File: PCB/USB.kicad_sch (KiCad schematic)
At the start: 13 parts, among them U8 LT1963AEST-3.3#TRPBF

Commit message: switching to hall effect for now
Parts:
- removed U8: LT1963AEST-3.3#TRPBF, Package_TO_SOT_SMD:SOT-223-3_TabPin2, symbol Regulator_Linear:LT1963AxST-3.3
- added U?: TLV1117-33, symbol Regulator_Linear:TLV1117-33
- C10, C7: value 10u -> 1u
- R1, R?: value R_US -> 5.1k
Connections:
- net +3.3V: now also U?.2 (VO)
- net +5V: now also U?.3 (VI)
- net GND: now also U?.1 (GND)
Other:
- note added: "5V to 3.3V LDO 1A max, bypass caps from data sheet"
- note removed: "5V to 3.3V LDO for ESP power from USB 1A max, bypass cap values via data sheet"
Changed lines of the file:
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@@
 		)
 	)
-	(text "5V to 3.3V LDO for ESP power from USB\n1A max, bypass cap values via data sheet "
+	(text "5V to 3.3V LDO\n1A max, bypass caps from data sheet"
 		(exclude_from_sim no)
 		(at 189.738 51.181 0)
@@
 	(wire
 		(pts
-			(xy 189.23 40.005) (xy 189.23 41.275)
+			(xy 189.23 37.465) (xy 189.23 41.275)
 		)
 		(stroke
@@
 	(wire
 		(pts
-			(xy 199.39 29.845) (xy 203.2 29.845)
-		)
-		(stroke
-			(width 0)
-			(type default)
-		)
-	)
-	(wire
-		(pts
 			(xy 50.8 33.02) (xy 57.15 33.02)
 		)
@@
 	(wire
 		(pts
+			(xy 196.85 29.845) (xy 203.2 29.845)
+		)
+		(stroke
+			(width 0)
+			(type default)
+		)
+	)
+	(wire
+		(pts
 			(xy 79.375 36.83) (xy 79.375 45.72)
 		)
@@
 	(wire
 		(pts
-			(xy 173.99 29.845) (xy 179.07 29.845)
+			(xy 173.99 29.845) (xy 181.61 29.845)
 		)
 		(stroke
@@
 			)
 		)
-		(property "Value" "R_US"
+		(property "Value" "5.1k"
 			(at 101.6 50.7999 0)
 			(effects
@@
 	)
 	(symbol
-		(lib_id "Regulator_Linear:LT1963AxST-3.3")
-		(at 189.23 32.385 0)
-		(unit 1)
-		(exclude_from_sim no)
-		(in_bom yes)
-		(on_board yes)
-		(dnp no)
-		(fields_autoplaced yes)
-		(property "Reference" "U8"
-			(at 189.23 22.225 0)
-			(effects
-				(font
-					(size 1.27 1.27)
-				)
-			)
-		)
-		(property "Value" "LT1963AEST-3.3#TRPBF"
-			(at 189.23 24.765 0)
-			(effects
-				(font
-					(size 1.27 1.27)
-				)
-			)
-		)
-		(property "Footprint" "Package_TO_SOT_SMD:SOT-223-3_TabPin2"
-			(at 189.23 43.815 0)
-			(effects
-				(font
-					(size 1.27 1.27)
-				)
-				(hide yes)
-			)
-		)
-		(property "Datasheet" "https://www.analog.com/media/en/technical-documentation/data-sheets/1963aff.pdf"
-			(at 189.23 46.355 0)
-			(effects
-				(font
-					(size 1.27 1.27)
-				)
-				(hide yes)
-			)
-		)
-		(property "Description" "3.3V, 1.5A, Low Noise, Fast Transient Response LDO Regulator, SOT-223"
-			(at 189.23 32.385 0)
-			(effects
-				(font
-					(size 1.27 1.27)
-				)
-				(hide yes)
-			)
-		)
-		(property "P/N" "LT1963AEST-3.3#TRPBF"
-			(at 189.23 32.385 0)
-			(effects
-				(font
-					(size 1.27 1.27)
-				)
-				(hide yes)
-			)
-		)
-		(property "Mouser Part Number" "584-1963AEST-3.3TPF"
-			(at 189.23 32.385 0)
-			(effects
-				(font
-					(size 1.27 1.27)
-				)
-				(hide yes)
-			)
-		)
-		(pin "2"
-		)
-		(pin "3"
-		)
-		(pin "1"
-		)
-		(instances
-			(project "OTCboard"
-				(path "/f410b0a0-725c-464e-80be-c0074224226d/df99ead2-0367-4be2-bcea-c49e7e835d17"
-					(reference "U8")
-					(unit 1)
-				)
-			)
-		)
-	)
-	(symbol
 		(lib_id "power:GND")
 		(at 99.695 54.61 0)
@@
 	)
 	(symbol
+		(lib_id "Regulator_Linear:TLV1117-33")
+		(at 189.23 29.845 0)
+		(unit 1)
+		(exclude_from_sim no)
+		(in_bom yes)
+		(on_board yes)
+		(dnp no)
+		(fields_autoplaced yes)
+		(property "Reference" "U?"
+			(at 189.23 22.86 0)
+			(effects
+				(font
+					(size 1.27 1.27)
+				)
+			)
+		)
+		(property "Value" "TLV1117-33"
+			(at 189.23 25.4 0)
+			(effects
+				(font
+					(size 1.27 1.27)
+				)
+			)
+		)
+		(property "Footprint" ""
+			(at 189.23 29.845 0)
+			(effects
+				(font
+					(size 1.27 1.27)
+				)
+				(hide yes)
+			)
+		)
+		(property "Datasheet" "http://www.ti.com/lit/ds/symlink/tlv1117.pdf"
+			(at 189.23 29.845 0)
+			(effects
+				(font
+					(size 1.27 1.27)
+				)
+				(hide yes)
+			)
+		)
+		(property "Description" "800mA Low-Dropout Linear Regulator, 3.3V fixed output, TO-220/TO-252/TO-263/SOT-223"
+			(at 189.23 29.845 0)
+			(effects
+				(font
+					(size 1.27 1.27)
+				)
+				(hide yes)
+			)
+		)
+		(pin "3"
+		)
+		(pin "1"
+		)
+		(pin "2"
+		)
+		(instances
+			(project ""
+				(path "/f410b0a0-725c-464e-80be-c0074224226d/df99ead2-0367-4be2-bcea-c49e7e835d17"
+					(reference "U?")
+					(unit 1)
+				)
+			)
+		)
+	)
+	(symbol
 		(lib_id "Device:LED")
 		(at 267.335 43.815 90)
@@
 			)
 		)
-		(property "Value" "R_US"
+		(property "Value" "5.1k"
 			(at 110.49 50.7999 0)
 			(effects
@@
 			)
 		)
-		(property "Value" "10u"
+		(property "Value" "1u"
 			(at 206.375 36.195 0)
 			(effects
@@
 			)
 		)
-		(property "Value" "10u"
+		(property "Value" "1u"
 			(at 177.165 36.1949 0)
 			(effects

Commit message: cramming for portfolio
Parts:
- J1: renamed from J?; footprint (none) -> Connector_USB:USB_C_Receptacle_GCT_USB4105-xx-A_16P_TopMnt_Horizontal
- R2: renamed from R?; footprint (none) -> Resistor_SMD:R_0603_1608Metric_Pad0.98x0.95mm_HandSolder
- R3: renamed from R1; footprint (none) -> Resistor_SMD:R_0603_1608Metric_Pad0.98x0.95mm_HandSolder
- U2: renamed from U?; footprint (none) -> Package_TO_SOT_SMD:SOT-223
- renumbered C13 to C4, C7 to C5, C10 to C6, D4 to D1, D1 to D2, D2 to D3, D3 to D4, R6 to R4, R7 to R5
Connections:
- net 5V_USB is gone; now on net +5V: C4.1

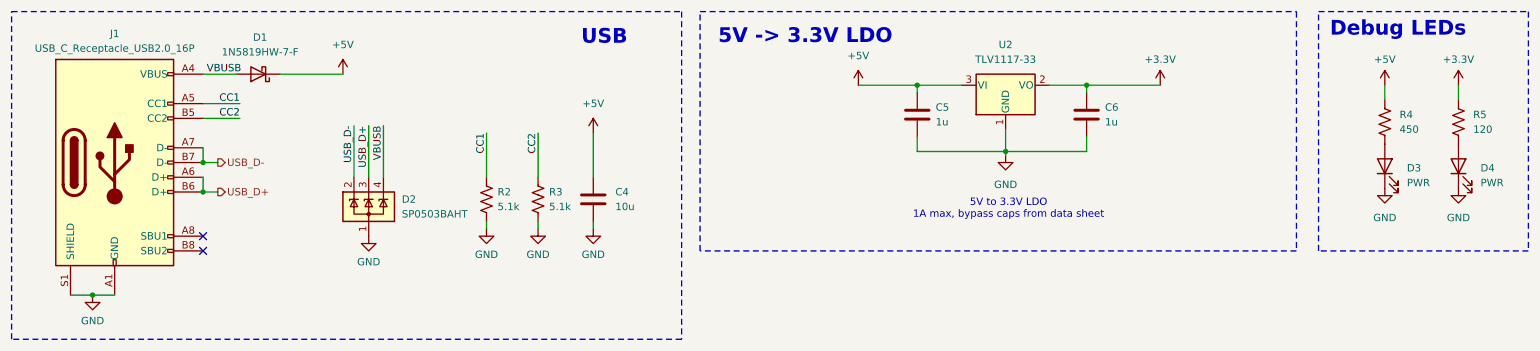
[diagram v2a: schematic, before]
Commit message: only need to find boot and reset footprints
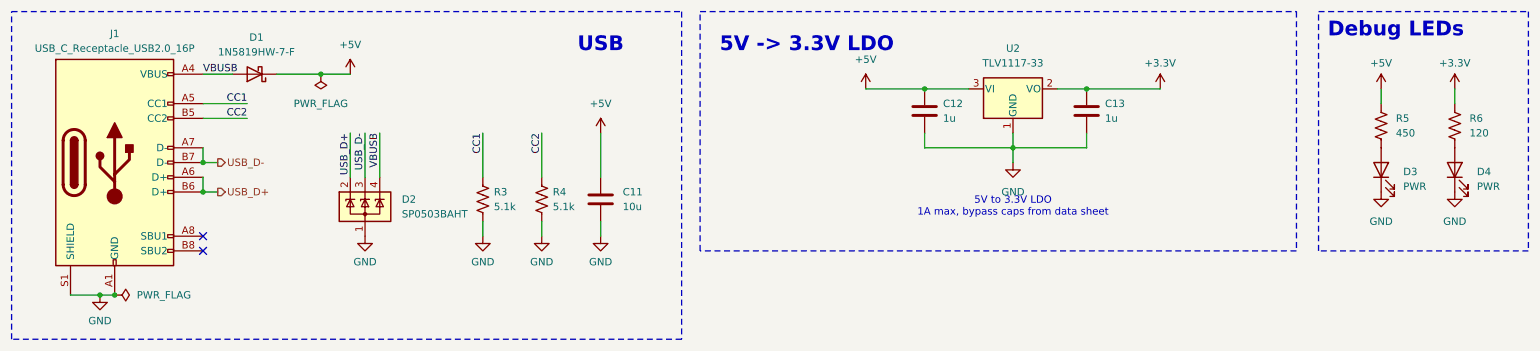
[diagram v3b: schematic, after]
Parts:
- removed D2: SP0503BAHT, Package_TO_SOT_SMD:SOT-143, symbol UTSVT_ICs:SP0503BAH
- added D2: SP0503BAHT, Package_TO_SOT_SMD:SOT-143, symbol Power_Protection:SP0503BAHT
- C12: renamed from C5; footprint Capacitor_SMD:C_0805_2012Metric_Pad1.18x1.45mm_HandSolder -> Capacitor_SMD:C_0603_1608Metric_Pad1.08x0.95mm_HandSolder
- C13: renamed from C6; footprint Capacitor_SMD:C_0805_2012Metric_Pad1.18x1.45mm_HandSolder -> Capacitor_SMD:C_0603_1608Metric_Pad1.08x0.95mm_HandSolder
- renumbered C4 to C11, R2 to R3, R3 to R4, R4 to R5, R5 to R6
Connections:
- net GND: now also D2.1 (A)
- net USB_D+: now also D2.2 (K)
- net USB_D-: now also D2.3 (K)
- net VBUSB: now also D2.4 (K)
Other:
- moved on the sheet: C11, C12, C13, D1, D3, D4, R3, R4, R5, R6, U2

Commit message: changing to wasd
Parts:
- removed U2: TLV1117-33, Package_TO_SOT_SMD:SOT-223, symbol Regulator_Linear:TLV1117-33
- added U2: MCP1826S, Package_TO_SOT_SMD:SOT-223-3_TabPin2, symbol Regulator_Linear:MCP1826S
- C11: renamed from C12; value 1u -> 10u
- C12: renamed from C13; value 1u -> 10u
- R5: value 450 -> 1k
- R6: value 120 -> 1k
- renumbered C11 to C10
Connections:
- net +3.3V: now also U2.3 (VO)
- net +5V: now also U2.1 (VI)
- net GND: now also U2.2 (GND)
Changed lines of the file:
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@@
-	(wire
-		(pts
-			(xy 190.5 43.18) (xy 190.5 40.64)
-		)
-		(stroke
-			(width 0)
-			(type default)
-		)
-	)
 	(wire
 		(pts
@@
 			)
 		)
-		(property "Value" "450"
+		(property "Value" "1k"
 			(at 256.54 38.0999 0)
 			(effects
@@
 			)
 		)
-		(property "Value" "120"
+		(property "Value" "1k"
 			(at 269.24 38.0999 0)
 			(effects
@@
 	)
 	(symbol
-		(lib_id "Regulator_Linear:TLV1117-33")
-		(at 190.5 30.48 0)
-		(unit 1)
-		(exclude_from_sim no)
-		(in_bom yes)
-		(on_board yes)
-		(dnp no)
-		(fields_autoplaced yes)
-		(property "Reference" "U2"
-			(at 190.5 23.495 0)
-			(effects
-				(font
-					(size 1.27 1.27)
-				)
-			)
-		)
-		(property "Value" "TLV1117-33"
-			(at 190.5 26.035 0)
-			(effects
-				(font
-					(size 1.27 1.27)
-				)
-			)
-		)
-		(property "Footprint" "Package_TO_SOT_SMD:SOT-223"
-			(at 190.5 30.48 0)
-			(effects
-				(font
-					(size 1.27 1.27)
-				)
-				(hide yes)
-			)
-		)
-		(property "Datasheet" "http://www.ti.com/lit/ds/symlink/tlv1117.pdf"
-			(at 190.5 30.48 0)
-			(effects
-				(font
-					(size 1.27 1.27)
-				)
-				(hide yes)
-			)
-		)
-		(property "Description" "800mA Low-Dropout Linear Regulator, 3.3V fixed output, TO-220/TO-252/TO-263/SOT-223"
-			(at 190.5 30.48 0)
-			(effects
-				(font
-					(size 1.27 1.27)
-				)
-				(hide yes)
-			)
-		)
-		(pin "3"
-		)
-		(pin "1"
-		)
-		(pin "2"
-		)
-		(instances
-			(project ""
-				(path "/f410b0a0-725c-464e-80be-c0074224226d/df99ead2-0367-4be2-bcea-c49e7e835d17"
-					(reference "U2")
-					(unit 1)
-				)
-			)
-		)
-	)
-	(symbol
 		(lib_id "Device:LED")
 		(at 266.7 44.45 90)
@@
 	)
 	(symbol
+		(lib_id "Regulator_Linear:MCP1826S")
+		(at 190.5 30.48 0)
+		(unit 1)
+		(exclude_from_sim no)
+		(in_bom yes)
+		(on_board yes)
+		(dnp no)
+		(fields_autoplaced yes)
+		(property "Reference" "U2"
+			(at 190.5 24.13 0)
+			(effects
+				(font
+					(size 1.27 1.27)
+				)
+			)
+		)
+		(property "Value" "MCP1826S"
+			(at 190.5 26.67 0)
+			(effects
+				(font
+					(size 1.27 1.27)
+				)
+			)
+		)
+		(property "Footprint" "Package_TO_SOT_SMD:SOT-223-3_TabPin2"
+			(at 187.96 26.67 0)
+			(effects
+				(font
+					(size 1.27 1.27)
+				)
+				(hide yes)
+			)
+		)
+		(property "Datasheet" "http://ww1.microchip.com/downloads/en/DeviceDoc/22057B.pdf"
+			(at 190.5 24.13 0)
+			(effects
+				(font
+					(size 1.27 1.27)
+				)
+				(hide yes)
+			)
+		)
+		(property "Description" "1000mA, Low-Voltage, Low Quiescent Current LDO Regulator, SOT-223, TO-220, TO-263"
+			(at 190.5 30.48 0)
+			(effects
+				(font
+					(size 1.27 1.27)
+				)
+				(hide yes)
+			)
+		)
+		(pin "2"
+		)
+		(pin "1"
+		)
+		(pin "3"
+		)
+		(instances
+			(project ""
+				(path "/f410b0a0-725c-464e-80be-c0074224226d/df99ead2-0367-4be2-bcea-c49e7e835d17"
+					(reference "U2")
+					(unit 1)
+				)
+			)
+		)
+	)
+	(symbol
 		(lib_id "Power_Protection:SP0503BAHT")
 		(at 78.74 50.8 0)
@@
 	(symbol
 		(lib_id "power:GND")
-		(at 190.5 43.18 0)
+		(at 190.5 40.64 0)
 		(unit 1)
 		(exclude_from_sim no)
@@
 		(fields_autoplaced yes)
 		(property "Reference" "#PWR028"
-			(at 190.5 49.53 0)
+			(at 190.5 46.99 0)
 			(effects
 				(font
@@
 		)
 		(property "Value" "GND"
-			(at 190.5 48.26 0)
+			(at 190.5 45.72 0)
 			(effects
 				(font
@@
 		)
 		(property "Footprint" ""
-			(at 190.5 43.18 0)
+			(at 190.5 40.64 0)
 			(effects
 				(font
@@
 		)
 		(property "Datasheet" ""
-			(at 190.5 43.18 0)
+			(at 190.5 40.64 0)
 			(effects
 				(font
@@
 		)
 		(property "Description" "Power symbol creates a global label with name \"GND\" , ground"
-			(at 190.5 43.18 0)
+			(at 190.5 40.64 0)
 			(effects
 				(font
@@
 		(on_board yes)
 		(dnp no)
-		(property "Reference" "C13"
+		(property "Reference" "C12"
 			(at 206.375 33.02 0)
 			(effects
@@
 			)
 		)
-		(property "Value" "1u"
+		(property "Value" "10u"
 			(at 206.375 35.56 0)
 			(effects
@@
 			(project "OTCboard"
 				(path "/f410b0a0-725c-464e-80be-c0074224226d/df99ead2-0367-4be2-bcea-c49e7e835d17"
-					(reference "C13")
+					(reference "C12")
 					(unit 1)
 				)
@@
 		(dnp no)
 		(fields_autoplaced yes)
-		(property "Reference" "C11"
+		(property "Reference" "C10"
 			(at 123.19 48.2599 0)
 			(effects
@@
 			(project "OTCboard"
 				(path "/f410b0a0-725c-464e-80be-c0074224226d/df99ead2-0367-4be2-bcea-c49e7e835d17"
-					(reference "C11")
+					(reference "C10")
 					(unit 1)
 				)
@@
 		(on_board yes)
 		(dnp no)
-		(property "Reference" "C12"
+		(property "Reference" "C11"
 			(at 178.435 33.02 0)
 			(effects
@@
 			)
 		)
-		(property "Value" "1u"
+		(property "Value" "10u"
 			(at 178.435 35.5599 0)
 			(effects
@@
 			(project "OTCboard"
 				(path "/f410b0a0-725c-464e-80be-c0074224226d/df99ead2-0367-4be2-bcea-c49e7e835d17"
-					(reference "C12")
-					(unit 1)
-				)
+					(reference "C11")
+					(unit 1)
+				)

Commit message: new update
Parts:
- added TP1, TP2: TestPoint, TestPoint:TestPoint_Loop_D2.54mm_Drill1.5mm_Beaded, symbol Connector:TestPoint
- C11, C12: footprint Capacitor_SMD:C_0603_1608Metric_Pad1.08x0.95mm_HandSolder -> Capacitor_SMD:C_0805_2012Metric_Pad1.18x1.45mm_HandSolder
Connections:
- net +3.3V: now also TP2.1
- net +5V: now also TP1.1
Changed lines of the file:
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@@
+		(color 0 0 0 0)
+	)
+	(junction
+		(at 76.2 27.94)
+		(diameter 0)
 		(color 0 0 0 0)
 	)
@@
 			)
 		)
-		(property "Footprint" "Capacitor_SMD:C_0603_1608Metric_Pad1.08x0.95mm_HandSolder"
+		(property "Footprint" "Capacitor_SMD:C_0805_2012Metric_Pad1.18x1.45mm_HandSolder"
 			(at 204.1652 38.1 0)
 			(effects
@@
 	)
 	(symbol
+		(lib_id "Connector:TestPoint")
+		(at 76.2 27.94 180)
+		(unit 1)
+		(exclude_from_sim no)
+		(in_bom yes)
+		(on_board yes)
+		(dnp no)
+		(fields_autoplaced yes)
+		(property "Reference" "TP1"
+			(at 78.74 29.9719 0)
+			(effects
+				(font
+					(size 1.27 1.27)
+				)
+				(justify right)
+			)
+		)
+		(property "Value" "TestPoint"
+			(at 78.74 32.5119 0)
+			(effects
+				(font
+					(size 1.27 1.27)
+				)
+				(justify right)
+			)
+		)
+		(property "Footprint" "TestPoint:TestPoint_Loop_D2.54mm_Drill1.5mm_Beaded"
+			(at 71.12 27.94 0)
+			(effects
+				(font
+					(size 1.27 1.27)
+				)
+				(hide yes)
+			)
+		)
+		(property "Datasheet" "~"
+			(at 71.12 27.94 0)
+			(effects
+				(font
+					(size 1.27 1.27)
+				)
+				(hide yes)
+			)
+		)
+		(property "Description" "test point"
+			(at 76.2 27.94 0)
+			(effects
+				(font
+					(size 1.27 1.27)
+				)
+				(hide yes)
+			)
+		)
+		(pin "1"
+		)
+		(instances
+			(project ""
+				(path "/f410b0a0-725c-464e-80be-c0074224226d/df99ead2-0367-4be2-bcea-c49e7e835d17"
+					(reference "TP1")
+					(unit 1)
+				)
+			)
+		)
+	)
+	(symbol
 		(lib_id "power:GND")
 		(at 33.02 66.04 0)
@@
 	)
 	(symbol
+		(lib_id "Connector:TestPoint")
+		(at 203.2 30.48 0)
+		(unit 1)
+		(exclude_from_sim no)
+		(in_bom yes)
+		(on_board yes)
+		(dnp no)
+		(fields_autoplaced yes)
+		(property "Reference" "TP2"
+			(at 205.105 25.9079 0)
+			(effects
+				(font
+					(size 1.27 1.27)
+				)
+				(justify left)
+			)
+		)
+		(property "Value" "TestPoint"
+			(at 205.105 28.4479 0)
+			(effects
+				(font
+					(size 1.27 1.27)
+				)
+				(justify left)
+			)
+		)
+		(property "Footprint" "TestPoint:TestPoint_Loop_D2.54mm_Drill1.5mm_Beaded"
+			(at 208.28 30.48 0)
+			(effects
+				(font
+					(size 1.27 1.27)
+				)
+				(hide yes)
+			)
+		)
+		(property "Datasheet" "~"
+			(at 208.28 30.48 0)
+			(effects
+				(font
+					(size 1.27 1.27)
+				)
+				(hide yes)
+			)
+		)
+		(property "Description" "test point"
+			(at 203.2 30.48 0)
+			(effects
+				(font
+					(size 1.27 1.27)
+				)
+				(hide yes)
+			)
+		)
+		(pin "1"
+		)
+		(instances
+			(project "OTCboard"
+				(path "/f410b0a0-725c-464e-80be-c0074224226d/df99ead2-0367-4be2-bcea-c49e7e835d17"
+					(reference "TP2")
+					(unit 1)
+				)
+			)
+		)
+	)
+	(symbol
 		(lib_id "Device:C")
 		(at 175.26 34.29 0)
@@
 			)
 		)
-		(property "Footprint" "Capacitor_SMD:C_0603_1608Metric_Pad1.08x0.95mm_HandSolder"
+		(property "Footprint" "Capacitor_SMD:C_0805_2012Metric_Pad1.18x1.45mm_HandSolder"
 			(at 176.2252 38.1 0)
 			(effects
